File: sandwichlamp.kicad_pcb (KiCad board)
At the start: 2 copper layers, 96 x 96 mm, 27 parts, among them J1 Pole1, J2 Pole2, J3 Pole3, J4 12V Enable, J5 HLK-LD2410C, J6 Conn_01x02, J7 Conn_01x03, SW1 Rader Power, SW3 POWER, U1 magnetic-charger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

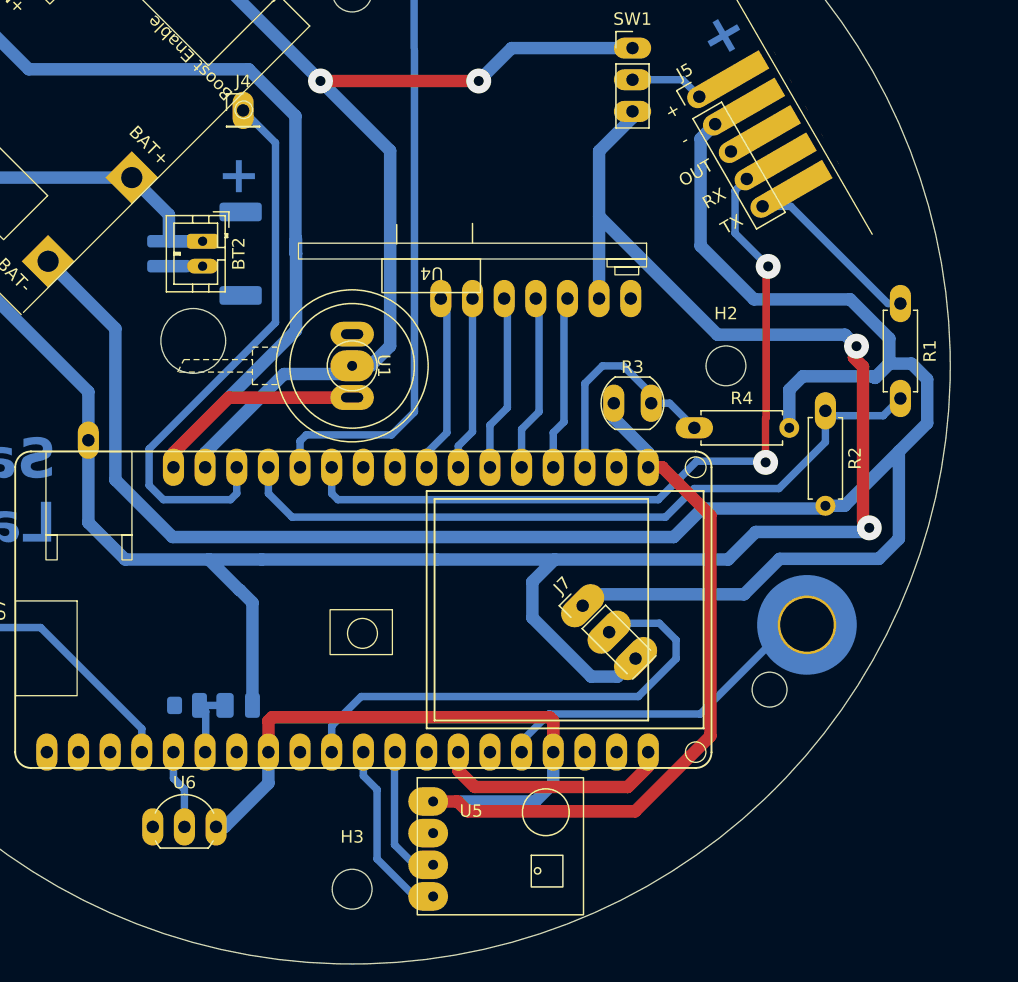
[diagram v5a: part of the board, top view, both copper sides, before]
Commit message: Relocate the light sensor so that it can actually sense some light from the top of the lamp
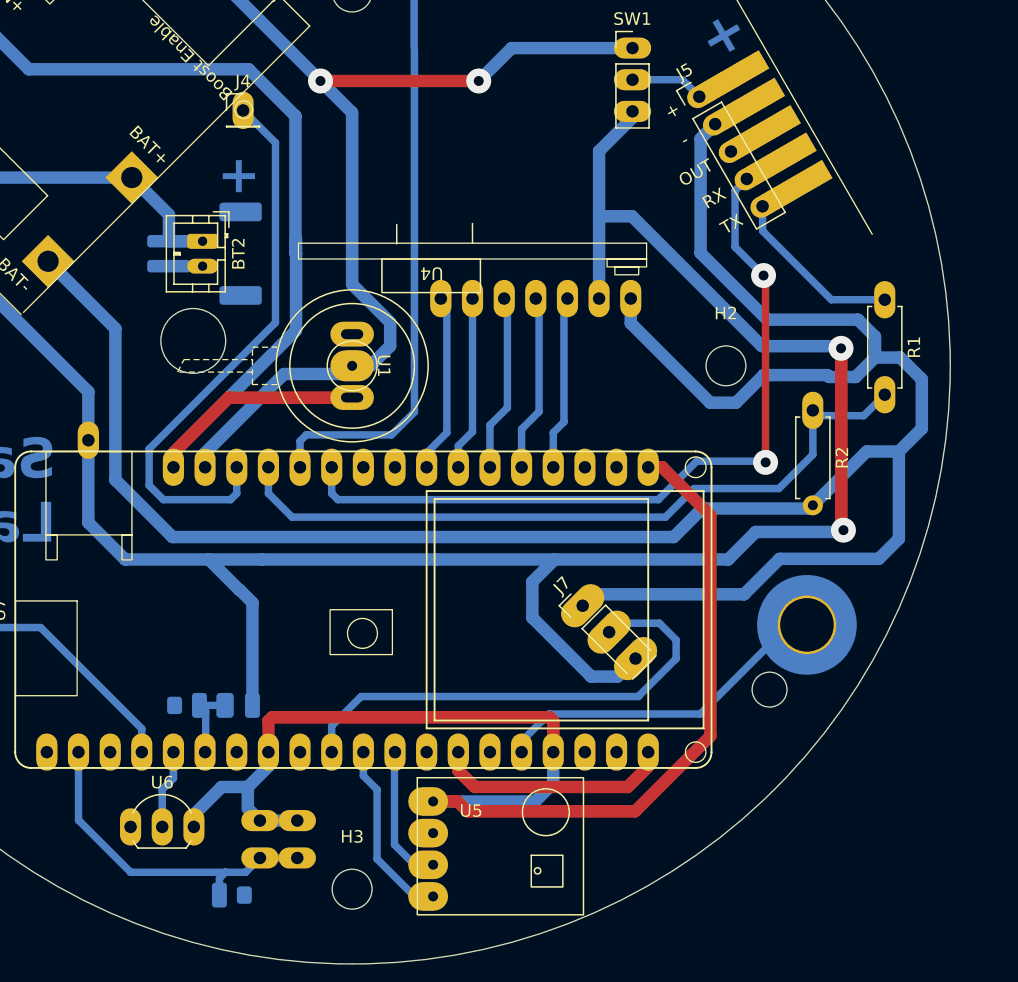
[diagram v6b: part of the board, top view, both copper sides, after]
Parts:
- R3: moved to B.Cu
- R4: footprint Resistor_THT:R_Axial_DIN0207_L6.3mm_D2.5mm_P7.62mm_Horizontal -> Resistor_SMD:R_0805_2012Metric_Pad1.20x1.40mm_HandSolder; moved to B.Cu
- moved R4 52.8 mm to (90.3, 142.5)
- moved R3 43.9 mm to (92.6, 136.5), turned to -90 degrees
- moved U6 1.78 mm to (82.2, 137.0)
- moved R1 1.29 mm to (142.7, 94.7)
- moved R2 1.01 mm to (137.0, 103.6)
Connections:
- U7 pad 3: Brightness -> unconnected-(U7-36/VP-Pad3)
- U7 pad 35: unconnected-(U7-2-Pad35) -> Brightness
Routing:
- net GND: track 290.8 -> 302.5 mm
- net Brightness: track 18.6 -> 27.3 mm
- net +4V: track 187.3 -> 183.5 mm
- net +3V3: track 104.7 -> 106.0 mm

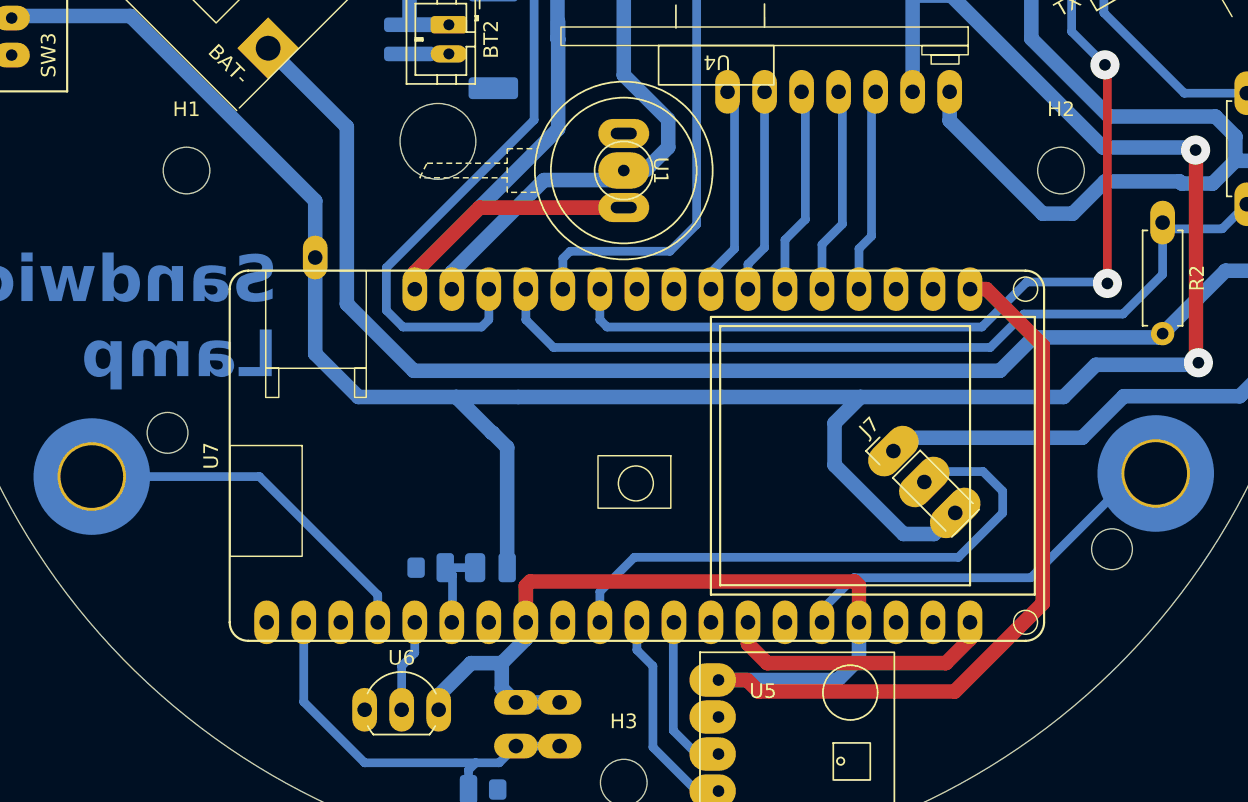
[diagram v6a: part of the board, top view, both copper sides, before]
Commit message: Fix the touch buttons
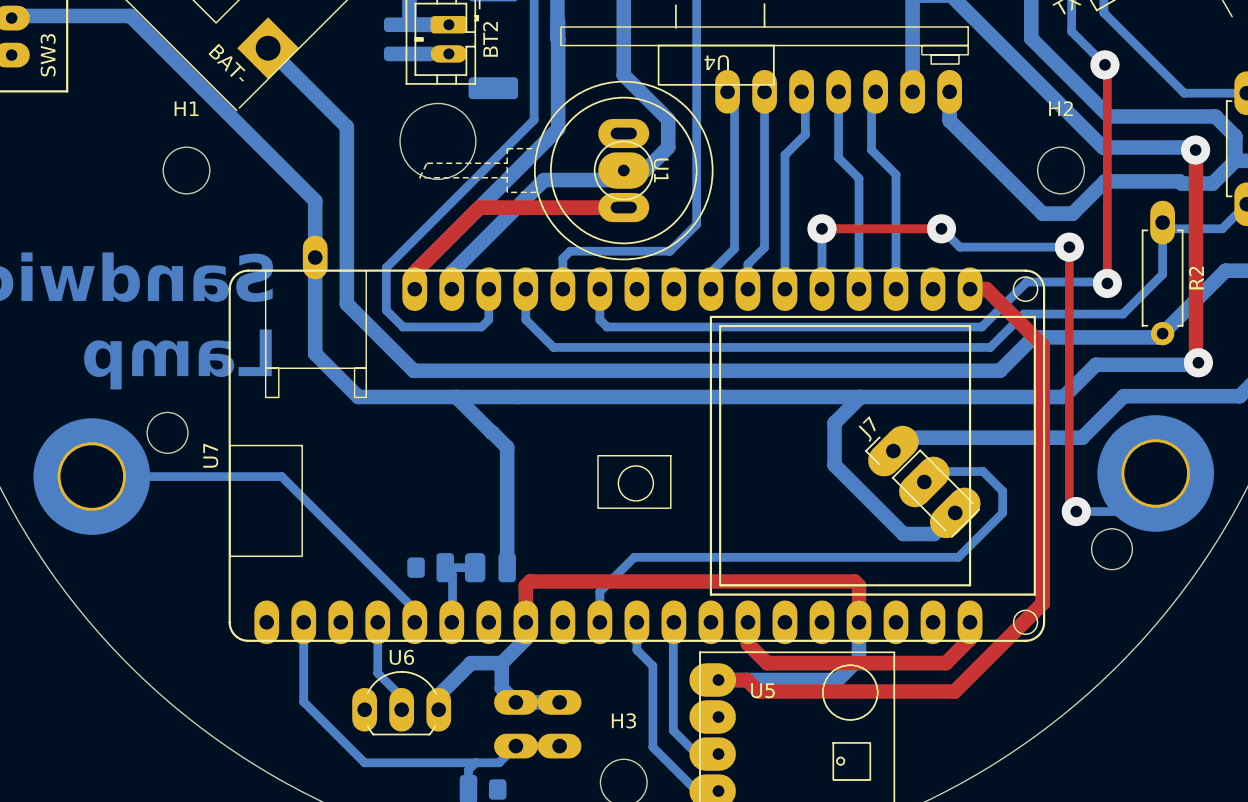
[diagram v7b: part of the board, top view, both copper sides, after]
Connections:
- U7 pad 21: Touch2 -> unconnected-(U7-SCL/22-Pad21)
- U7 pad 3: unconnected-(U7-36/VP-Pad3) -> Button4
- U7 pad 32: OneWire -> Touch3
- U7 pad 33: Touch3 -> OneWire
- U7 pad 37: +4V -> (no net)
- U7 pad 4: Button4 -> Button3
- U7 pad 5: Button3 -> Touch2
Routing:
- net Touch2: track 27.6 -> 46.5 mm, vias 0 -> 4
- net Touch3: track 24.9 -> 26.8 mm
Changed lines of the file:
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@@
 	(net 13 "OneWire")
 	(net 14 "unconnected-(SW3-C-Pad3)")
-	(net 15 "unconnected-(U7-36{slash}VP-Pad3)")
+	(net 15 "unconnected-(U7-SCL{slash}22-Pad21)")
 	(net 16 "unconnected-(U7-26-Pad10)")
 	(net 17 "unconnected-(U7-25-Pad9)")
@@
 			(layers "*.Cu" "*.Mask")
 			(remove_unused_layers no)
-			(net 15 "unconnected-(U7-36{slash}VP-Pad3)")
-			(pinfunction "36/VP")
-			(pintype "bidirectional")
+			(net 11 "Button4")
+			(pinfunction "I36/VP")
+			(pintype "input")
 		)
 		(pad "4" thru_hole oval
@@
 			(layers "*.Cu" "*.Mask")
 			(remove_unused_layers no)
-			(net 11 "Button4")
-			(pinfunction "39/VN")
-			(pintype "bidirectional")
+			(net 9 "Button3")
+			(pinfunction "I39/VN")
+			(pintype "input")
 		)
 		(pad "5" thru_hole oval
@@
 			(layers "*.Cu" "*.Mask")
 			(remove_unused_layers no)
-			(net 9 "Button3")
+			(net 21 "Touch2")
 			(pinfunction "32")
 			(pintype "bidirectional")
@@
 			(remove_unused_layers no)
 			(net 10 "Button1")
-			(pinfunction "34")
-			(pintype "bidirectional")
+			(pinfunction "I34")
+			(pintype "input")
 		)
 		(pad "8" thru_hole oval
@@
 			(remove_unused_layers no)
 			(net 27 "ButtonX")
-			(pinfunction "35")
-			(pintype "bidirectional")
+			(pinfunction "I35")
+			(pintype "input")
 		)
 		(pad "9" thru_hole oval
@@
 			(layers "*.Cu" "*.Mask")
 			(remove_unused_layers no)
-			(net 21 "Touch2")
+			(net 15 "unconnected-(U7-SCL{slash}22-Pad21)")
 			(pinfunction "SCL/22")
 			(pintype "bidirectional")
@@
 			(layers "*.Cu" "*.Mask")
 			(remove_unused_layers no)
-			(net 13 "OneWire")
+			(net 22 "Touch3")
 			(pinfunction "4")
 			(pintype "bidirectional")
@@
 			(layers "*.Cu" "*.Mask")
 			(remove_unused_layers no)
-			(net 22 "Touch3")
+			(net 13 "OneWire")
 			(pinfunction "0")
 			(pintype "bidirectional")
@@
 			(layers "*.Cu" "*.Mask")
 			(remove_unused_layers no)
-			(net 3 "+4V")
-			(pinfunction "BAT")
-			(pintype "input")
 		)
 		(model "${KIPRJMOD}/lib/lolin32/lolin32.step"
@@
 		(tags "resistor handsolder")
 		(property "Reference" "R4"
-			(at 0 1.65 360)
+			(at 0 1.65 0)
 			(layer "B.SilkS")
 			(effects
@@
 		)
 		(property "Value" "10k"
-			(at 0 -1.65 360)
+			(at 0 -1.65 0)
 			(layer "B.Fab")
 			(effects
@@
 		)
 		(fp_text user "${REFERENCE}"
-			(at 0 0 360)
+			(at 0 0 0)
 			(layer "B.Fab")
 			(effects
@@
 	)
 	(segment
-		(start 113.6 105.08)
-		(end 113.6 108.14)
-		(width 0.6)
-		(layer "B.Cu")
-		(net 9)
-	)
-	(segment
 		(start 114.74 94.6)
-		(end 115 94.86)
+		(end 114.74 99.14)
 		(width 0.6)
 		(layer "B.Cu")
@@
 	)
 	(segment
-		(start 115 94.86)
-		(end 115 103.68)
+		(start 114.74 99.14)
+		(end 116.14 100.54)
 		(width 0.6)
 		(layer "B.Cu")
@@
 	)
 	(segment
-		(start 115 103.68)
-		(end 113.6 105.08)
+		(start 116.14 100.54)
+		(end 116.14 108.14)
 		(width 0.6)
 		(layer "B.Cu")
@@
 	)
 	(segment
-		(start 116.14 105.36)
-		(end 117 104.5)
+		(start 117.28 94.6)
+		(end 117 94.88)
 		(width 0.6)
 		(layer "B.Cu")
@@
 	)
 	(segment
-		(start 117 104.5)
-		(end 117 94.88)
+		(start 117 98.6)
+		(end 118.68 100.28)
 		(width 0.6)
 		(layer "B.Cu")
@@
 	)
 	(segment
-		(start 116.14 108.14)
-		(end 116.14 105.36)
+		(start 117 94.88)
+		(end 117 98.6)
 		(width 0.6)
 		(layer "B.Cu")
@@
 	)
 	(segment
-		(start 117 94.88)
-		(end 117.28 94.6)
+		(start 118.68 100.28)
+		(end 118.68 108.14)
 		(width 0.6)
 		(layer "B.Cu")
@@
 	)
 	(segment
-		(start 112.46 103.36)
-		(end 111.06 104.76)
+		(start 112.46 94.86)
+		(end 112.46 97.54)
 		(width 0.6)
 		(layer "B.Cu")
@@
 	)
 	(segment
-		(start 112.46 94.86)
-		(end 112.46 103.36)
+		(start 112.2 94.6)
+		(end 112.46 94.86)
 		(width 0.6)
 		(layer "B.Cu")
@@
 	)
 	(segment
-		(start 111.06 104.76)
-		(end 111.06 108.14)
+		(start 112.46 97.54)
+		(end 111.06 98.94)
 		(width 0.6)
 		(layer "B.Cu")
@@
 	)
 	(segment
-		(start 112.2 94.6)
-		(end 112.46 94.86)
+		(start 111.06 98.94)
+		(end 111.06 108.14)
 		(width 0.6)
 		(layer "B.Cu")
@@
 	)
 	(segment
-		(start 85.66 131)
-		(end 85.66 133.1)
+		(start 83.12 134.492284)
+		(end 84.76 136.132284)
 		(width 0.6)
 		(layer "B.Cu")
@@
 	)
 	(segment
-		(start 85.66 133.1)
-		(end 84.76 134)
+		(start 83.12 131)
+		(end 83.12 134.492284)
 		(width 0.6)
 		(layer "B.Cu")
@@
 	)
 	(segment
-		(start 84.76 134)
+		(start 84.76 136.132284)
 		(end 84.76 137)
 		(width 0.6)
@@
 	)
 	(segment
-		(start 127.935 127.94)
-		(end 135.0875 120.7875)
+		(start 130.57502 105.258676)
+		(end 130.57502 122.92502)
 		(width 0.6)
-		(layer "B.Cu")
+		(layer "F.Cu")
 		(net 21)
 	)
 	(segment
-		(start 135.0875 120.7875)
+		(start 113.6 104)
+		(end 121.8 104)
+		(width 0.6)
+		(layer "F.Cu")
+		(net 21)
+	)
+	(segment
+		(start 130.57502 122.92502)
+		(end 131.05 123.4)
+		(width 0.6)
+		(layer "F.Cu")
+		(net 21)
+	)
+	(via
+		(at 130.57502 105.258676)
+		(size 2)
+		(drill 0.8)
+		(layers "F.Cu" "B.Cu")
+		(net 21)
+	)
+	(via
+		(at 131.05 123.4)
+		(size 2)
+		(drill 0.8)
+		(layers "F.Cu" "B.Cu")
+		(net 21)
+	)
+	(via
+		(at 113.6 104)
+		(size 2)
+		(drill 0.8)
+		(layers "F.Cu" "B.Cu")
+		(net 21)
+	)
+	(via
+		(at 121.8 104)
+		(size 2)
+		(drill 0.8)
+		(layers "F.Cu" "B.Cu")
+		(net 21)
+	)
+	(segment
+		(start 133.8875 123.4)
 		(end 136.5 120.7875)
 		(width 0.6)
@@
 	)
 	(segment
-		(start 113.6 131)
-		(end 113.6 130.132284)
+		(start 123.058676 105.258676)
+		(end 130.57502 105.258676)
 		(width 0.6)
 		(layer "B.Cu")
@@
 	)
 	(segment
-		(start 113.6 130.132284)
-		(end 115.792284 127.94)
+		(start 113.6 108.14)
+		(end 113.6 104)
 		(width 0.6)
 		(layer "B.Cu")
@@
 	)
 	(segment
-		(start 115.792284 127.94)
-		(end 127.935 127.94)
+		(start 121.8 104)
+		(end 123.058676 105.258676)
 		(width 0.6)
 		(layer "B.Cu")
@@
 	)
 	(segment
-		(start 83.12 129.12)
-		(end 75 121)
+		(start 131.05 123.4)
+		(end 133.8875 123.4)
 		(width 0.6)
 		(layer "B.Cu")
-		(net 22)
+		(net 21)
 	)
 	(segment
-		(start 83.12 131)
-		(end 83.12 129.12)
+		(start 85.66 130.132284)
+		(end 76.527716 121)
 		(width 0.6)
 		(layer "B.Cu")
@@
 	)
 	(segment
-		(start 75 121)
+		(start 76.527716 121)
 		(end 63.5 121)
 		(width 0.6)
 		(layer "B.Cu")
+		(net 22)
+	)
+	(segment
+		(start 85.66 131)
+		(end 85.66 130.132284)
+		(width 0.6)
+		(layer "B.Cu")
